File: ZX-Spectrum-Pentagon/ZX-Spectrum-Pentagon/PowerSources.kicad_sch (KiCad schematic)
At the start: 69 parts

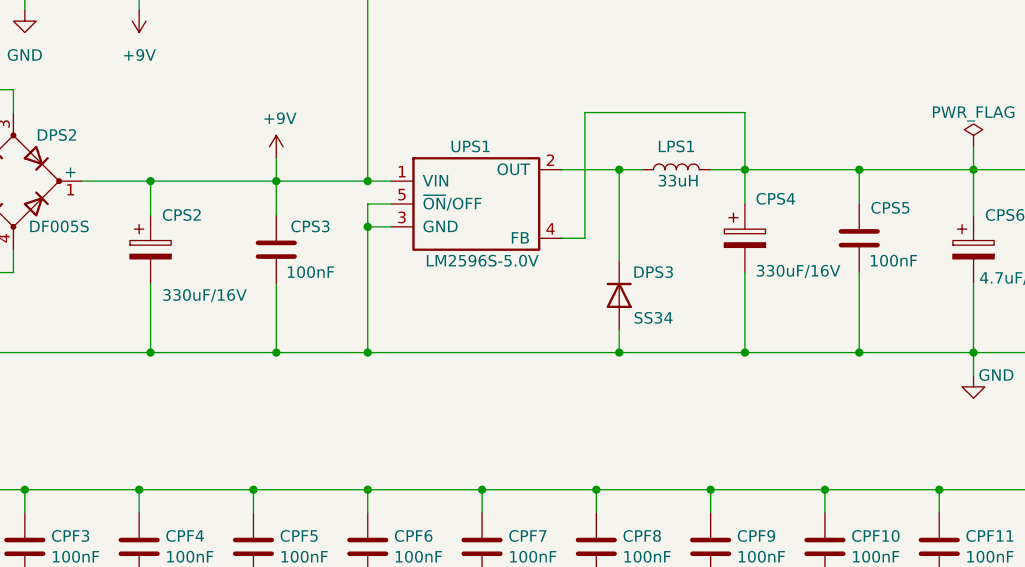
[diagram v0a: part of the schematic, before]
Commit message: improve schematic fdc
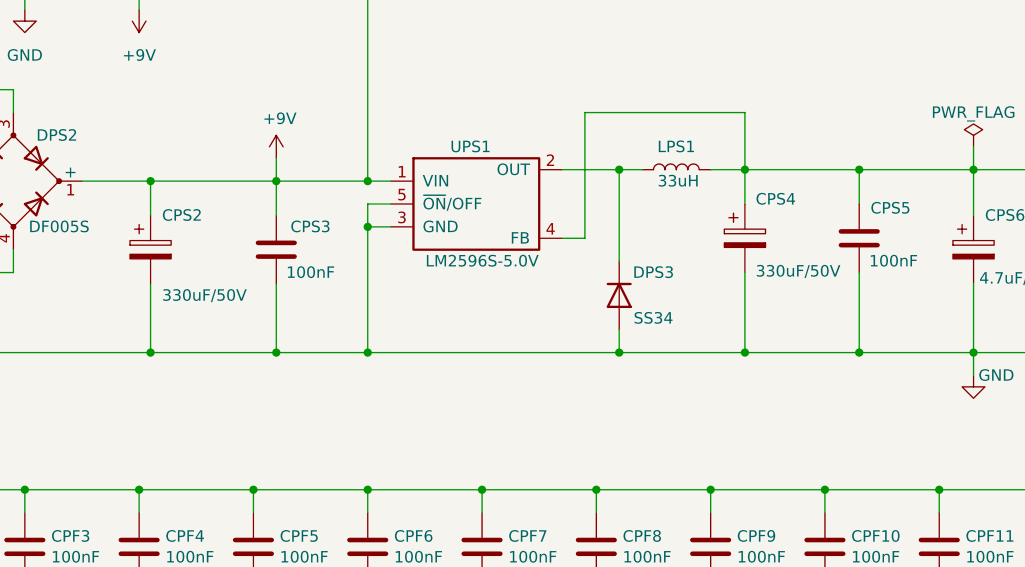
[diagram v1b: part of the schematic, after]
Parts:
- CPS2, CPS4: value 330uF/16V -> 330uF/50V
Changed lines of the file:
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@@
 			)
 		)
-		(property "Value" "330uF/16V"
+		(property "Value" "330uF/50V"
 			(at 66.04 59.69 0)
 			(effects
@@
 			)
 		)
-		(property "Value" "330uF/16V"
+		(property "Value" "330uF/50V"
 			(at 132 57 0)
 			(effects

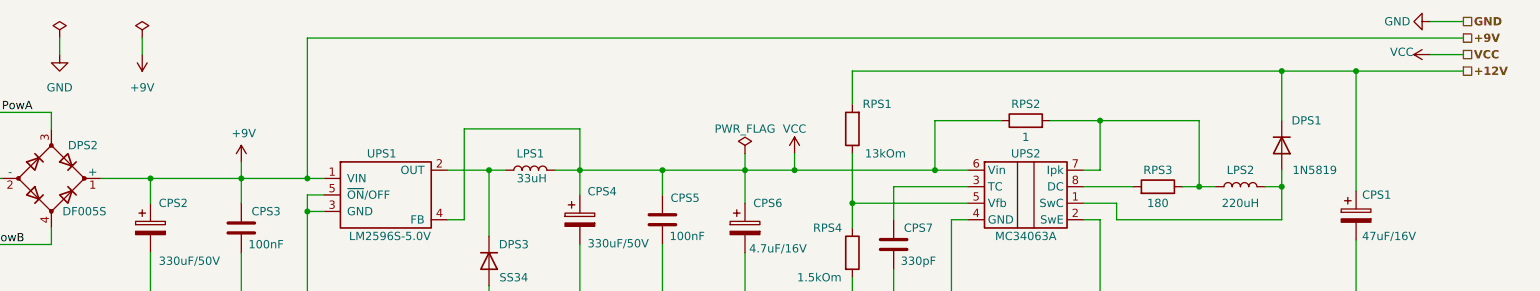
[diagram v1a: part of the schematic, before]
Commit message: FDControlers rename from VCC1 to VDD zx_custom_symbol add connector Conn_02x32_Odd_Even ZX-Spectrum-Pentagon rename from +9V to POWER ZX-Spectrum-Perefiral improve schematic
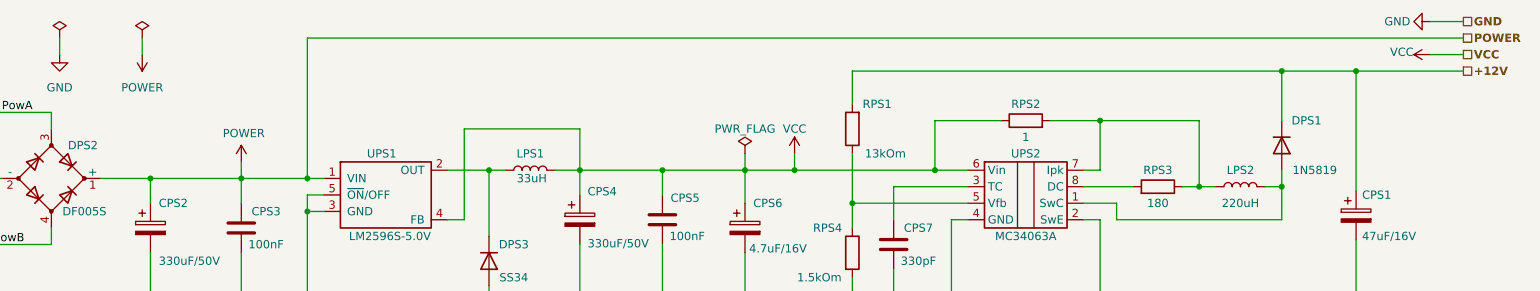
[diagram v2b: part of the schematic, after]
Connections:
- net +9V renamed POWER
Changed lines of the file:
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@@
 		)
 	)
-	(hierarchical_label "+9V"
+	(hierarchical_label "POWER"
 		(shape passive)
 		(at 266.7 25.4 0)
@@
 			)
 		)
-		(property "Value" "+9V"
+		(property "Value" "POWER"
 			(at 79.121 40.0558 0)
 			(effects
@@
 			)
 		)
-		(property "Value" "+9V"
+		(property "Value" "POWER"
 			(at 63.5 33.02 0)
 			(effects
